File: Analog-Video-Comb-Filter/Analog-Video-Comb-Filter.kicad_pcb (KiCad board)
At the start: 2 copper layers, 51.5 x 104.1 mm, 80 parts, among them J1 12VDC(+), J2 SVHS, J3 CV-OUT, J4 CV-IN, Q1 BC548, U1 L7805, U2 AD8044, U3 SAA4960/61, U4 MC44144, U5 74HC04, U6 LM1881, U7 SAA4963, Y1 See table

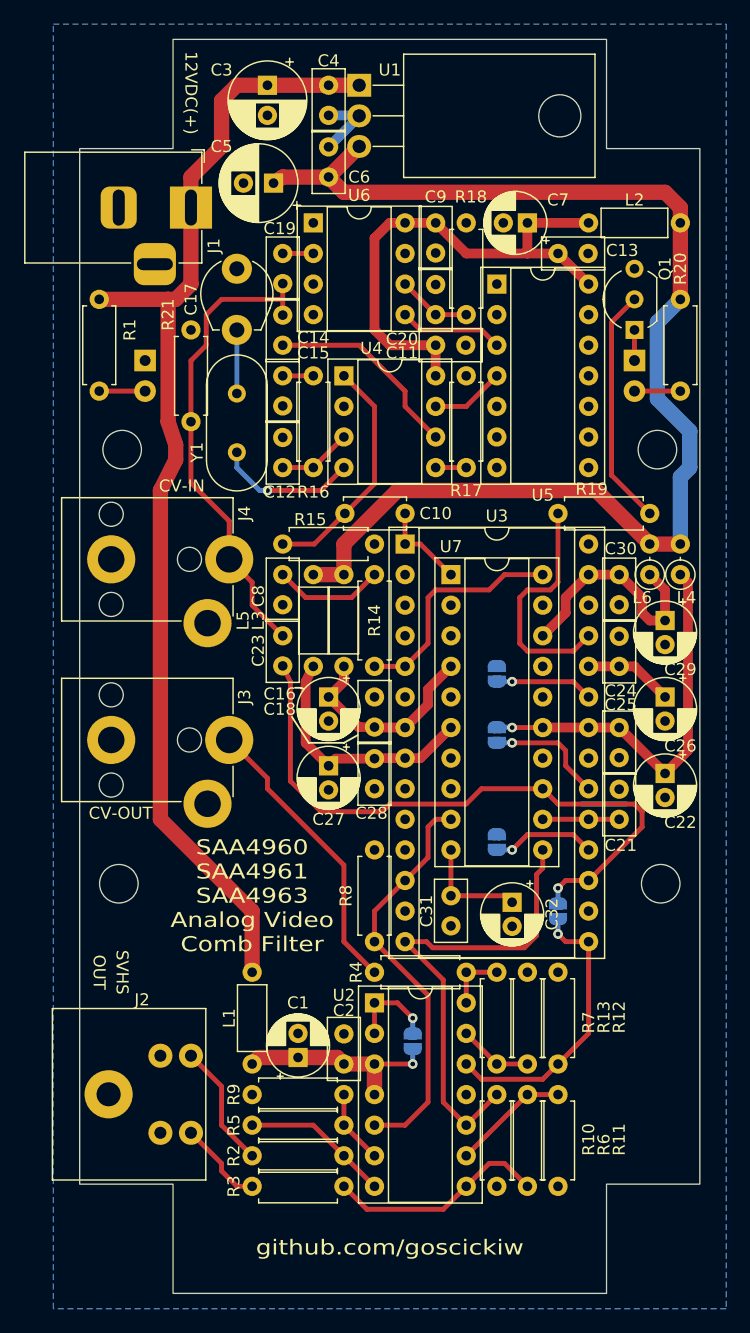
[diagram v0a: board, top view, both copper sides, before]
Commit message: Revision 3
- Settled on AD813 as the output amplifier, this should also fix #1 as AD8044 is no longer used;
- Added output gain adjustment.
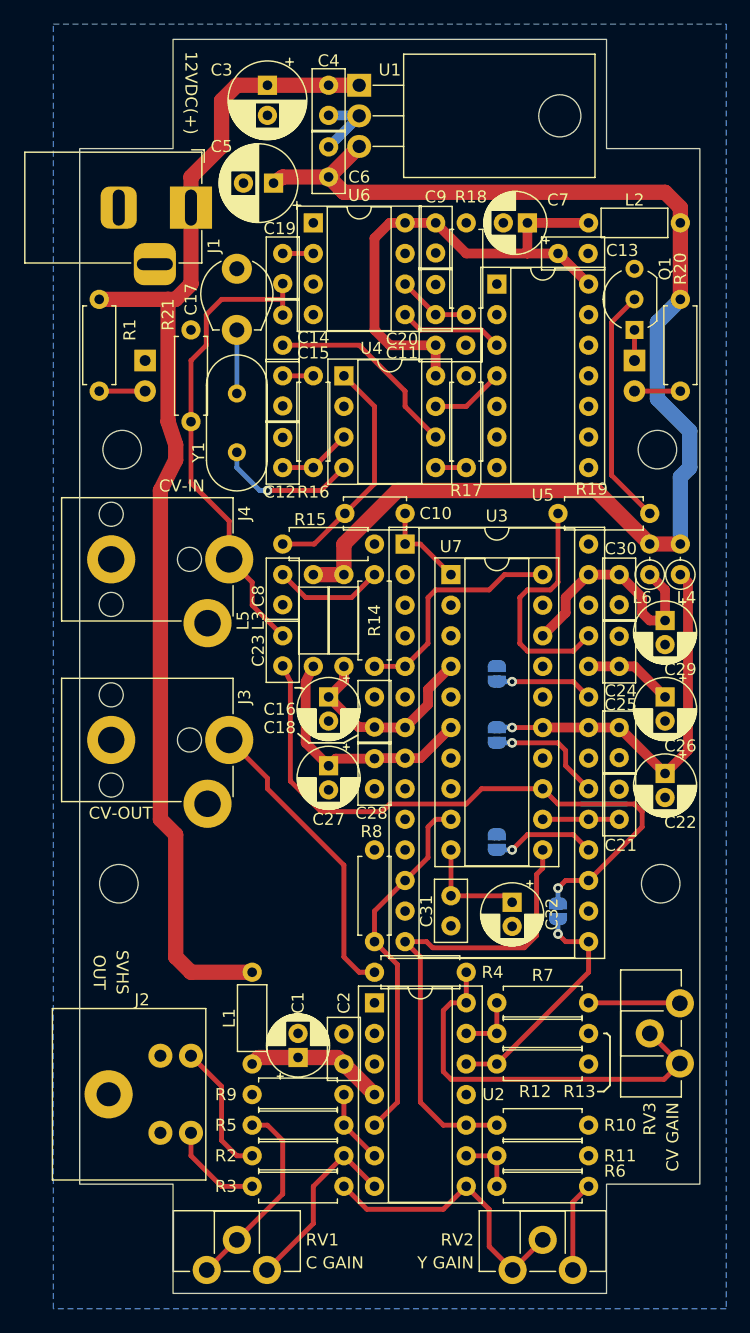
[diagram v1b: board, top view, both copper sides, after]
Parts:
- removed the JP1 at (149.2, 130.2)
- added RV1: 1k, Potentiometer_THT:Potentiometer_Piher_PT-10-H01_Horizontal, F.Cu at (132.1, 149.2)
- added RV2: 1k, Potentiometer_THT:Potentiometer_Piher_PT-10-H01_Horizontal, F.Cu at (157.5, 149.2)
- added RV3: 1k, Potentiometer_THT:Potentiometer_Piher_PT-10-H01_Horizontal, F.Cu at (171.4, 132.0)
- R5, R6, R7: value 1k -> 470R
- U2: value AD8044 -> AD813
- moved R7 8.03 mm to (163.8, 127.0), turned to 180 degrees
- moved R11 7.18 mm to (156.2, 139.7), turned to 0 degrees
- moved R6 5.08 mm to (163.8, 142.2), turned to 180 degrees
- moved R12 5.08 mm to (156.2, 132.1), turned to 0 degrees
- moved R13 3.59 mm to (156.2, 129.5), turned to 0 degrees
- moved R10 2.54 mm to (156.2, 137.2), turned to 0 degrees
- renumbered JP2 to JP1, JP3 to JP2, JP4 to JP3, JP5 to JP4
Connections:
- R5 pad 1: Net-(R2-Pad2) -> Net-(R5-Pad1)
- R6 pad 1: Net-(R3-Pad2) -> Net-(R6-Pad1)
- R7 pad 1: Net-(R4-Pad2) -> Net-(R7-Pad1)
- U2 pad 1: Net-(JP1-A) (its old number) -> unconnected-(U2A-~{DISABLE}-Pad1)
- U2 pad 2: Net-(JP1-A) (its old number) -> unconnected-(U2B-~{DISABLE}-Pad2)
- U2 pad 3: +12VA -> unconnected-(U2C-~{DISABLE}-Pad3)
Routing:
- net Net-(R4-Pad2): track 5.08 -> 33.8 mm
- net Net-(R5-Pad1): track 0.00 -> 16.4 mm
- net Net-(R7-Pad1): track 0.00 -> 7.60 mm
- net Net-(JP1-A) (its old number): track 7.51 -> 0.00 mm, vias 1 -> 0
- net Net-(R6-Pad1): track 0.00 -> 7.49 mm
- net +12VA: track 17.6 -> 11.7 mm, vias 1 -> 0
- net Net-(R3-Pad2): track 18.4 -> 23.8 mm
- net Net-(U2C--): track 9.72 -> 5.08 mm
- net /CVO: track 23.9 -> 19.9 mm
- net /CO: track 33.9 -> 30.4 mm
- net Net-(R2-Pad2): track 12.3 -> 15.7 mm
- net +12V: track 95.8 -> 98.8 mm
- net Net-(U2B--): track 6.13 -> 5.08 mm
- net /YL: track 7.29 -> 8.04 mm
- net /CVL: track 24.3 -> 25.0 mm
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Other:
- board text added: "Analog Video Comb Filter"
- board text removed: "OUT"
- board text removed: "SAA4960 SAA4961 SAA4963 Analog Video Comb Filter"
